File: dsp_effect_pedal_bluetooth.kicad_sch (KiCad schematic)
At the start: 5 parts, among them J1 USB_C_Receptacle_PowerOnly_24P

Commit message: input buffer
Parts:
- removed input_buf: TL072, symbol Amplifier_Operational:TL072
- added R1: 1M, symbol Device:R
- added U2: TL072IP, digikey-footprints:DIP-8_W7.62mm, symbol dk_Linear-Amplifiers-Instrumentation-OP-Amps-Buffer-Amps:TL072IP
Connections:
- net GND: now reaches J1.A1 (GND), J1.A12 (GND), J1.B1 (GND), J1.B12 (GND)
- net GND: now also AUX_IN.S, R1.2
- net at AUX_IN.T: now also R1.1, U2.2
- new net: U2.1, U2.3
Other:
- note added: "1M resistor bc guitar signal is AC coupled and we need stable DC reference voltage"
- note added: "buffer to isolate guitar signal whilst maintaining high input impedance. Prevents pickup loading & ensures signal integrity"
- moved on the sheet: AUX_IN

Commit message: step up converter work
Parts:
- added 1uF/25V: 1uF_0603_25V, 4ms_Capacitor:C_0603, symbol PCM_4ms_Capacitor:1uF_0603_25V
- added C1: 0.1uF_0603_16V, 4ms_Capacitor:C_0603, symbol PCM_4ms_Capacitor:0.1uF_0603_16V
- added L1: 10 uH, digikey-footprints:1206, symbol dk_Fixed-Inductors:82103C
- added R2: 10k_0603, 4ms_Resistor:R_0603, symbol PCM_4ms_Resistor:10k_0603
- added U1: MT3608, Package_TO_SOT_SMD:SOT-23-6, symbol Regulator_Switching:MT3608
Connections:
- net GND: now also 1uF/25V.2, C1.2, U1.2 (GND)
- net at J1.A4 (VBUS), J1.A9 (VBUS), J1.B4 (VBUS)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: now also 1uF/25V.1, C1.1, R2.1, U1.5 (IN)
- new net: L1.1, U1.1 (SW)
- new net: R2.2, U1.4 (EN)
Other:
- note added: "TODO: - adjustable gain for input OpAmp? - check caps. Maybe make components so better sizes? (learn to model) - vet the cap's ripple current. Assume ok for now"
- note added: "boost converter considerations: - effiency (9V @ 500mA => 5V @ 1.1A) - expected current load (600 mA max?) - noise and ripple - as long as current ripple <RMS of caps :) - picked 10uH inductor. should b overkill - schottky diode. Consider forward V drop, reverse voltage rating, forward I rating, switching speed"
- note added: "buffer considerations: - low bias - high input impedance"
- moved on the sheet: AUX_IN, AUX_OUT, J1, R1, U2A

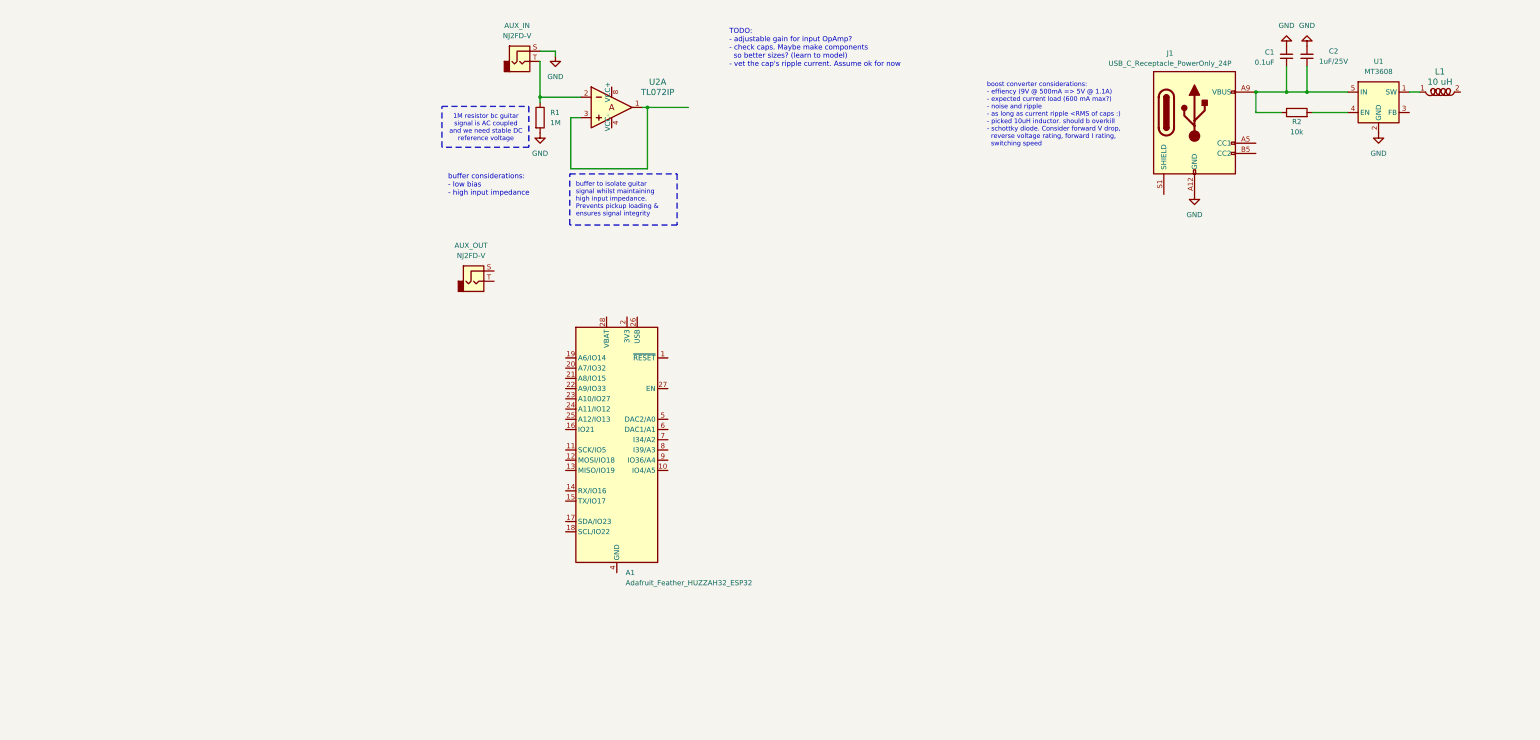
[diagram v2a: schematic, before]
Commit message: finished step up and analog input
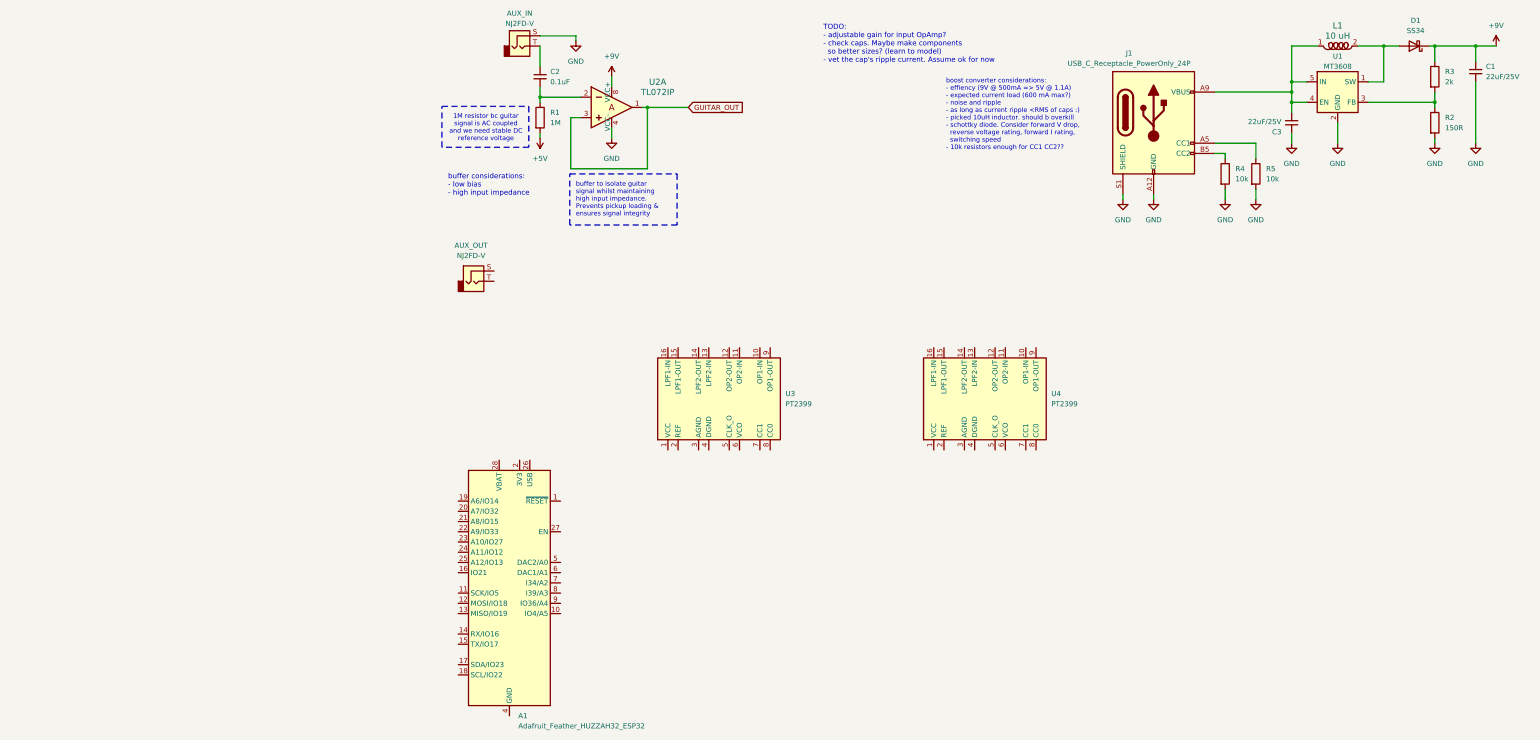
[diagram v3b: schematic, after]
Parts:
- removed 1uF/25V: 1uF_0603_25V, 4ms_Capacitor:C_0603, symbol PCM_4ms_Capacitor:1uF_0603_25V
- removed C1: 0.1uF_0603_16V, 4ms_Capacitor:C_0603, symbol PCM_4ms_Capacitor:0.1uF_0603_16V
- removed R2: 10k_0603, 4ms_Resistor:R_0603, symbol PCM_4ms_Resistor:10k_0603
- added C1, C3: 22uF_1206_25V, 4ms_Capacitor:C_1206, symbol PCM_4ms_Capacitor:22uF_1206_25V
- added C2: 100nF_0603_16V, 4ms_Capacitor:C_0603, symbol PCM_4ms_Capacitor:100nF_0603_16V
- added D1: SS34, Diode_SMD:D_SMA, symbol Diode:SS34
- added R2: 150R_0603, 4ms_Resistor:R_0603, symbol PCM_4ms_Resistor:150R_0603
- added R3: 2k_0603, 4ms_Resistor:R_0603, symbol PCM_4ms_Resistor:2k_0603
- added R4, R5: 10k_0603, 4ms_Resistor:R_0603, symbol PCM_4ms_Resistor:10k_0603
- added U3, U4: PT2399, Package_DIP:DIP-16_W7.62mm, symbol Audio:PT2399
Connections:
- net GND: now also J1.S1 (SHIELD), U2.4 (VCC-), C1.2, C3.1, R2.2, R4.2, R5.2; no longer R1.2
- net at U1.1 (SW): now also L1.2, D1.2 (A); no longer L1.1
- net at U1.3 (FB): now also R2.1, R3.2
- net at U1.4 (EN): now also J1.A4 (VBUS), J1.A9 (VBUS), J1.B4 (VBUS), J1.B9 (VBUS), L1.1, U1.5 (IN), C3.2
- net at J1.A5 (CC1): now also R5.1
- net at J1.B5 (CC2): now also R4.1
- net at R1.1, U2.2: now also C2.2; no longer AUX_IN.T
- net GUITAR_OUT: now reaches U2.1, U2.3
- net +9V: now reaches U2.8 (VCC+)
- net +9V: now also C1.1, D1.1 (K), R3.1
- new net: AUX_IN.T, C2.1
- new net +5V: R1.2
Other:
- note added: "boost converter considerations: - effiency (9V @ 500mA => 5V @ 1.1A) - expected current load (600 mA max?) - noise and ripple - as long as current ripple <RMS of caps :) - picked 10uH inductor. should b overkill - schottky diode. Consider forward V drop, reverse voltage rating, forward I rating, switching speed - 10k resistors enough for CC1 CC2??"
- note removed: "boost converter considerations: - effiency (9V @ 500mA => 5V @ 1.1A) - expected current load (600 mA max?) - noise and ripple - as long as current ripple <RMS of caps :) - picked 10uH inductor. should b overkill - schottky diode. Consider forward V drop, reverse voltage rating, forward I rating, switching speed"
- moved on the sheet: A1, AUX_IN, J1, L1, U1

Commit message: GIGA added. Delay stage + output adder schematics + hierarchy
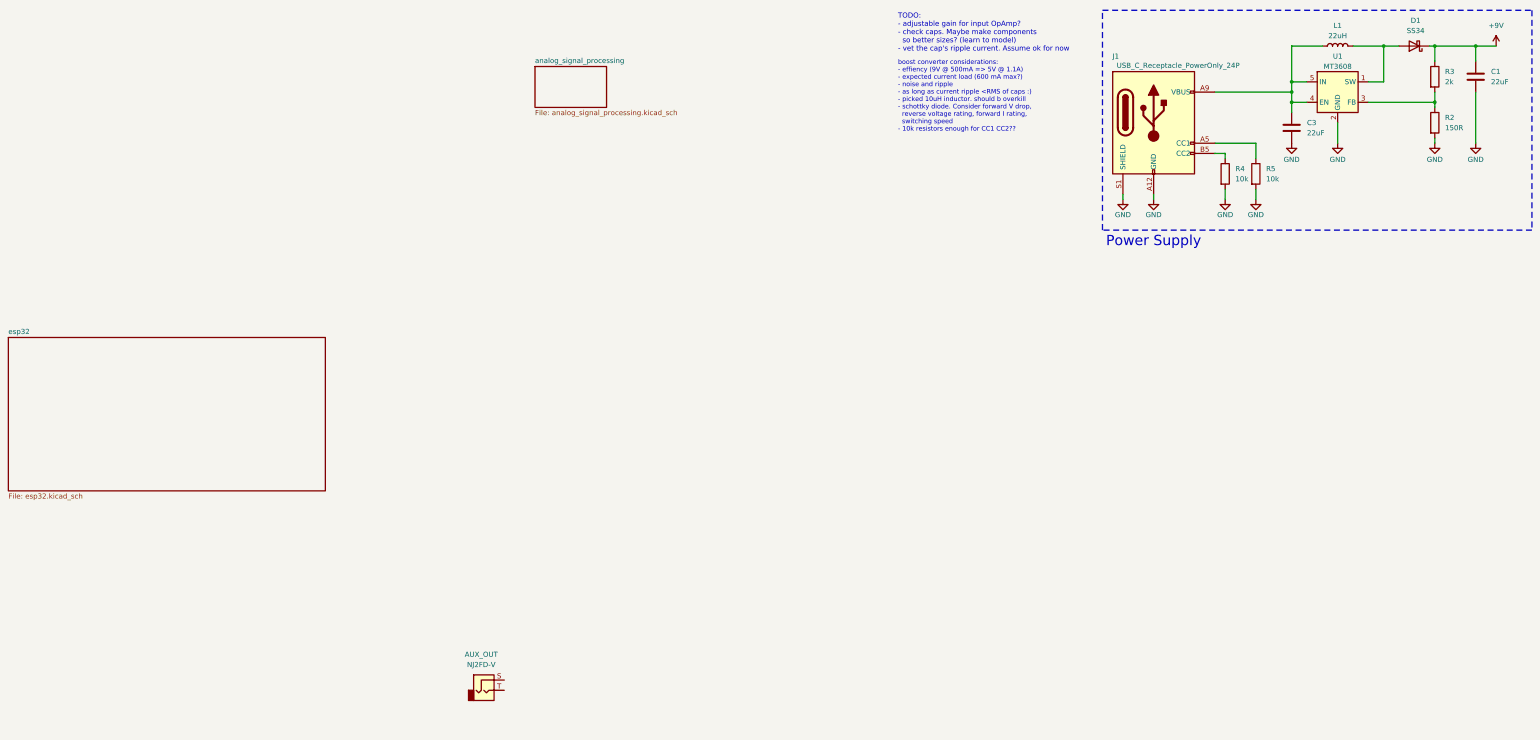
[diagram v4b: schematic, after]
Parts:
- removed A1: Adafruit_Feather_HUZZAH32_ESP32, Module:Adafruit_Feather, symbol MCU_Module:Adafruit_Feather_HUZZAH32_ESP32
- removed AUX_IN: NJ2FD-V, Connector_Audio:Jack_6.35mm_Neutrik_NJ2FD-V_Vertical, symbol Connector_Audio:NJ2FD-V
- removed C1, C3: 22uF_1206_25V, 4ms_Capacitor:C_1206, symbol PCM_4ms_Capacitor:22uF_1206_25V
- removed C2: 100nF_0603_16V, 4ms_Capacitor:C_0603, symbol PCM_4ms_Capacitor:100nF_0603_16V
- removed L1: 10 uH, digikey-footprints:1206, symbol dk_Fixed-Inductors:82103C
- removed R1: 1M, symbol Device:R
- removed U2: TL072IP, digikey-footprints:DIP-8_W7.62mm, symbol dk_Linear-Amplifiers-Instrumentation-OP-Amps-Buffer-Amps:TL072IP
- removed U3, U4: PT2399, Package_DIP:DIP-16_W7.62mm, symbol Audio:PT2399
- added C1, C3: 22uF, symbol Device:C
- added L1: 22uH, symbol Device:L
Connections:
- net +9V: now also C1.1
- net GND: now also C1.2, C3.2
- net at D1.2 (A), U1.1 (SW): now also L1.2
- net at J1.A4 (VBUS), J1.A9 (VBUS), J1.B4 (VBUS)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: now also C3.1, L1.1
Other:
- added sheet analog_signal_processing (analog_signal_processing.kicad_sch)
- added sheet esp32 (esp32.kicad_sch)
- note added: "Power Supply"
- note removed: "1M resistor bc guitar signal is AC coupled and we need stable DC reference voltage"
- note removed: "buffer considerations: - low bias - high input impedance"
- note removed: "buffer to isolate guitar signal whilst maintaining high input impedance. Prevents pickup loading & ensures signal integrity"
- moved on the sheet: AUX_OUT

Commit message: wip on esp conns
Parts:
- removed C1, C3: 22uF, symbol Device:C
- removed D1: SS34, Diode_SMD:D_SMA, symbol Diode:SS34
- removed J1: USB_C_Receptacle_PowerOnly_24P, symbol Connector:USB_C_Receptacle_PowerOnly_24P
- removed L1: 22uH, symbol Device:L
- removed R2: 150R_0603, 4ms_Resistor:R_0603, symbol PCM_4ms_Resistor:150R_0603
- removed R3: 2k_0603, 4ms_Resistor:R_0603, symbol PCM_4ms_Resistor:2k_0603
- removed R4, R5: 10k_0603, 4ms_Resistor:R_0603, symbol PCM_4ms_Resistor:10k_0603
- removed U1: MT3608, Package_TO_SOT_SMD:SOT-23-6, symbol Regulator_Switching:MT3608
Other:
- note removed: "Power Supply"
- note removed: "TODO: - adjustable gain for input OpAmp? - check caps. Maybe make components so better sizes? (learn to model) - vet the cap's ripple current. Assume ok for now"
- note removed: "boost converter considerations: - effiency (9V @ 500mA => 5V @ 1.1A) - expected current load (600 mA max?) - noise and ripple - as long as current ripple <RMS of caps :) - picked 10uH inductor. should b overkill - schottky diode. Consider forward V drop, reverse voltage rating, forward I rating, switching speed - 10k resistors enough for CC1 CC2??"

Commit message: fixed a lot of things
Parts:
- removed AUX_OUT: NJ2FD-V, Connector_Audio:Jack_6.35mm_Neutrik_NJ2FD-V_Vertical, symbol Connector_Audio:NJ2FD-V
- added A1: Adafruit_Feather_HUZZAH32_ESP32, Module:Adafruit_Feather, symbol MCU_Module:Adafruit_Feather_HUZZAH32_ESP32
- added C1, C33, C35: 47uF, CAPPRD200W50D525H1250, symbol SamacSys_Parts:REA470M1CBK-0511P
- added C29: 100nF, SR211C104KARTR1, symbol SamacSys_Parts:SR211C104KARTR1
- added C39, C40: 22uF, FG20, symbol SamacSys_Parts:FG20X7R1C226MRT06
- added D4: SS34, Diode_SMD:D_SMA, symbol Diode:SS34
- added ENC1: Encoder_Rotary_11mm_SPST_DShaft, 4ms_Encoder:ENC_SPST_12mm, symbol PCM_4ms_Switch:Encoder_Rotary_11mm_SPST_DShaft
- added J1, J4: 0022232041, digikey-footprints:PinHeader_1x4_P2.54mm_Drill1.02mm, symbol dk_Rectangular-Connectors-Headers-Male-Pins:0022232041
- added L2: 10uH_1.0A_4018, Inductor_SMD:L_Taiyo-Yuden_NR-40xx, symbol PCM_4ms_Inductor:10uH_1.0A_4018
- added LED1: HV-5RGB60, HV5RGB25, symbol SamacSys_Parts:HV-5RGB60
- added Q3, Q4: 2N5088BU_Obsolete, digikey-footprints:TO-92-3, symbol dk_Transistors-Bipolar-BJT-Single:2N5088BU_Obsolete
- added R2, R20, R21, R28, R3, R4, R5, R6: 4.7k, RESAD1590W60L630D240, symbol SamacSys_Parts:MFR-25FRF52-4K7
- added R29: 2k, RESAD1550W60L630D230, symbol SamacSys_Parts:YR1B2K0CC
- added R30: 150, RESAD1590W60L630D240, symbol SamacSys_Parts:MFR-25FBF52-150R
- added S1: SF17020F-0302-21R-L-015, SF17020F030221RL015, symbol SamacSys_Parts:SF17020F-0302-21R-L-015
- added U1: MCP6002-I_P, digikey-footprints:DIP-8_W7.62mm, symbol dk_Linear-Amplifiers-Instrumentation-OP-Amps-Buffer-Amps:MCP6002-I_P
- added U11: MT3608, Package_TO_SOT_SMD:SOT-23-6, symbol Regulator_Switching:MT3608
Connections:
- new net: Q3.1 (E), R2.2, U1.6
- new net: Q4.1 (E), R4.2, U1.2
- new net: C35.1, R21.2, R3.2, U1.5
- new net: Q3.2 (B), U1.7
- new net: D4.2 (A), L2.2, U11.1 (SW)
- new net: Q4.2 (B), U1.1
- new net: A1.14 (RX/IO16), LED1.1 (ANODE_BLUE)
- new net: A1.15 (TX/IO17), LED1.2 (ANODE_RED)
- new net: C1.1, R20.2, R5.2, U1.3
- new net: A1.21 (A8/IO15), ENC1.1
- new net: A1.23 (A10/IO27), ENC1.2
- new net: A1.25 (A12/IO13), ENC1.3
- new net: R29.2, R30.2, U11.3 (FB)
- new net: A1.19 (A6/IO14), ENC1.SW1
- new net +3V3: A1.2 (3V3), C39.2, J1.4, L2.1, U11.4 (EN), U11.5 (IN)
- new net +5V: C29.1, U1.8 (VSS), U1.8 (VSS)
- new net +9V: C40.2, D4.1 (K), J4.4, R29.1, R6.2
- new net 4.5V: C33.1, R28.2, R6.1
- new net AUDIO_IN: J4.2
- new net DELAY_CURRENT_0: Q3.3 (C)
- new net DELAY_CURRENT_1: Q4.3 (C)
- new net EFFECT_OUT: J4.3
- new net GND: A1.4 (GND), C1.2, C29.2, C33.2, C35.2, C39.1, C40.1, ENC1.SW2, J1.1, LED1.3 (COMMON_CATHODE), R2.1, R20.1, R28.1, R3.1, R30.1, R4.1, U1.4 (VDD), U1.4 (VDD), U11.2 (GND)
- new net PWM0: A1.20 (A7/IO32), R21.1
- new net PWM1: A1.22 (A9/IO33), R5.1
- new net RESET: A1.1 (~{RESET})
- new net U4A: A1.24 (A11/IO12)
- new net U4B: A1.5 (DAC2/A0)
- new net U4C: A1.28 (VBAT)
- new net U4D: A1.6 (DAC1/A1)
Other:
- removed sheet esp32
- note added: "2N5088 PBFREE == 2N5088U_Obsolete replacement"
- note added: "LED to be used for determine effect 'state'"
- note added: "Power Supply"
- note added: "TODO: - adjustable gain for input OpAmp? - check caps. Maybe make components so better sizes? (learn to model) - vet the cap's ripple current. Assume ok for now - add connectors to breakout signals"
- note added: "boost converter considerations: - effiency (9V @ 500mA => 5V @ 1.1A) - expected current load (600 mA max?) - noise and ripple - as long as current ripple <RMS of caps :) - picked 10uH inductor. should b overkill - schottky diode. Consider forward V drop, reverse voltage rating, forward I rating, switching speed - 10k resistors enough for CC1 CC2??"
